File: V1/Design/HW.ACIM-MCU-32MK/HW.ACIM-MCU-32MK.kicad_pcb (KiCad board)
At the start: 4 copper layers, 32 x 20 mm, 28 parts, among them J1 HEADER 2x15POS, J2 HEADER 2x15POS, U1 MIPS 32-bit DSC, U2 12MHz

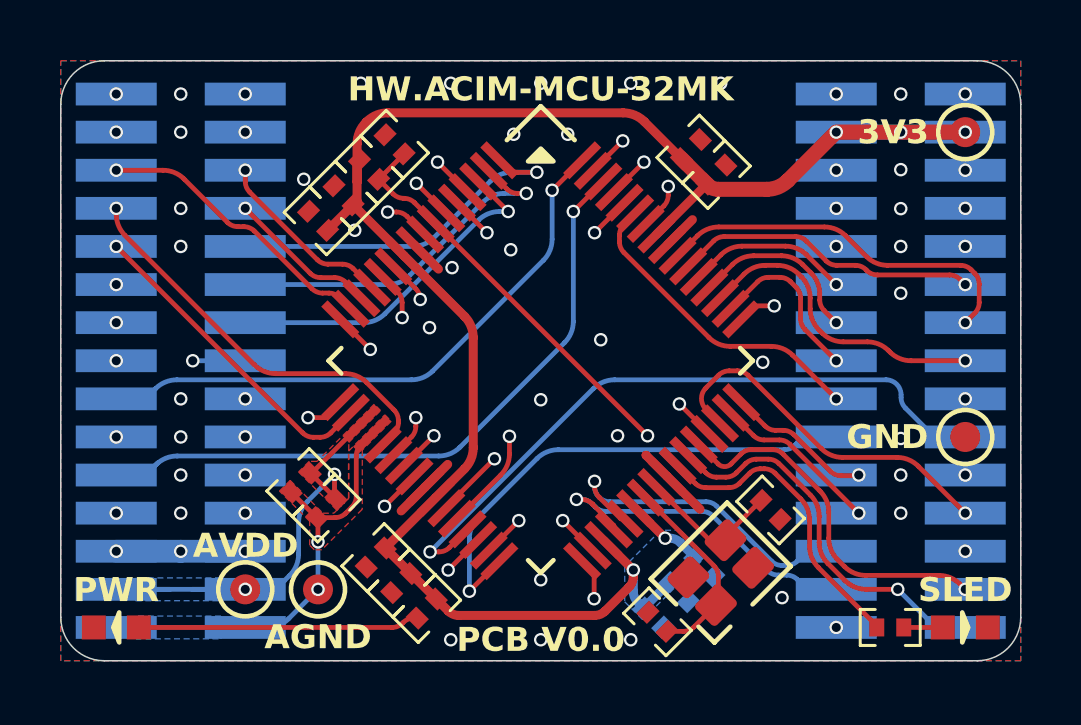
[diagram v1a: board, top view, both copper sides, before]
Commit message: HW.ACIM-MCU-32MK update net name
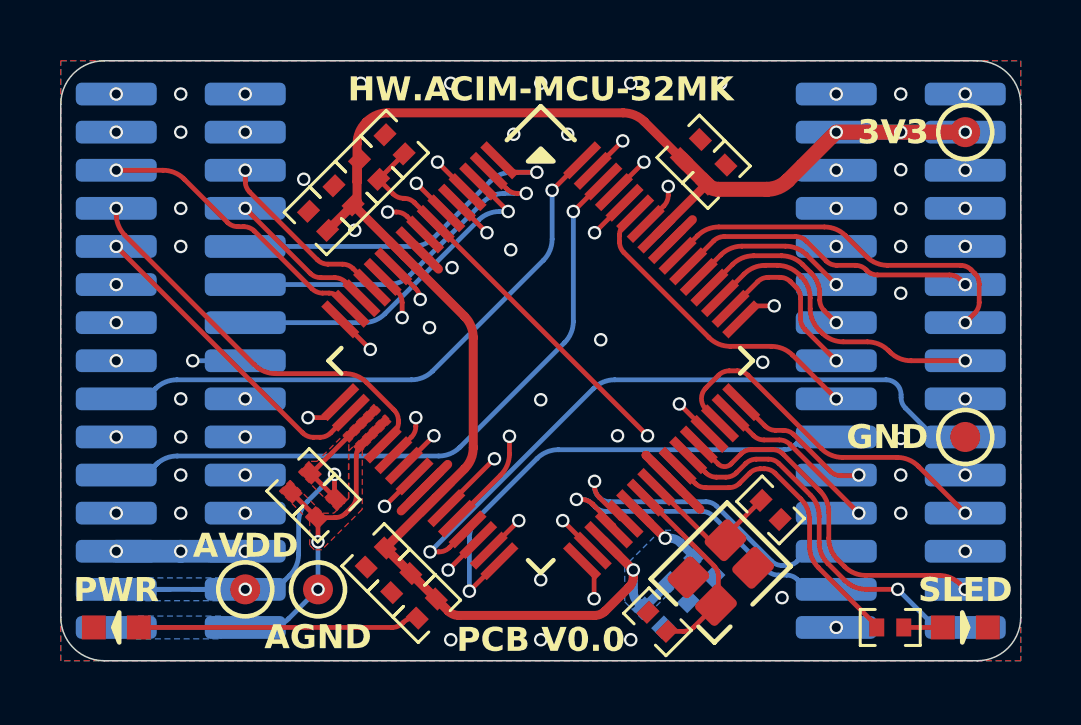
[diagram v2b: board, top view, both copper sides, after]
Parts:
- removed G***: LOGO, LOGO
- renumbered C1 to C101, C10 to C110, C12 to C112, C13 to C113, C19 to C119, C20 to C120, C21 to C121, C22 to C122, C23 to C123, C24 to C124, C25 to C125, C26 to C126, C27 to C127, C28 to C128, D1 to D101, D2 to D102, J1 to J101, J2 to J102, R1 to R101, R2 to R102, R3 to R103, TP1 to TP101, TP2 to TP102, TP3 to TP103, TP4 to TP104, U1 to U101, U2 to U102
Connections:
- net +3V3 renamed +3V3_ISO
- net AGND renamed AGND_ISO
- net AVDD renamed AVDD_ISO
- net GND renamed GND_ISO
